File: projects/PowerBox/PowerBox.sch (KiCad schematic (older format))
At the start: 45 parts, among them CON1 USB-MICRO, CON2 USB-MICRO, IC1 OPAMP-DUALU, IC2 ATTINY85-S, P1 CONN_2, P2 CONN_2, P3 CONN_1, P4 CONN_1, P5 CONN_1, P6 CONN_1, P7 CONN_3X2, U1 74HC595, U2 74HC595, U3 INA169

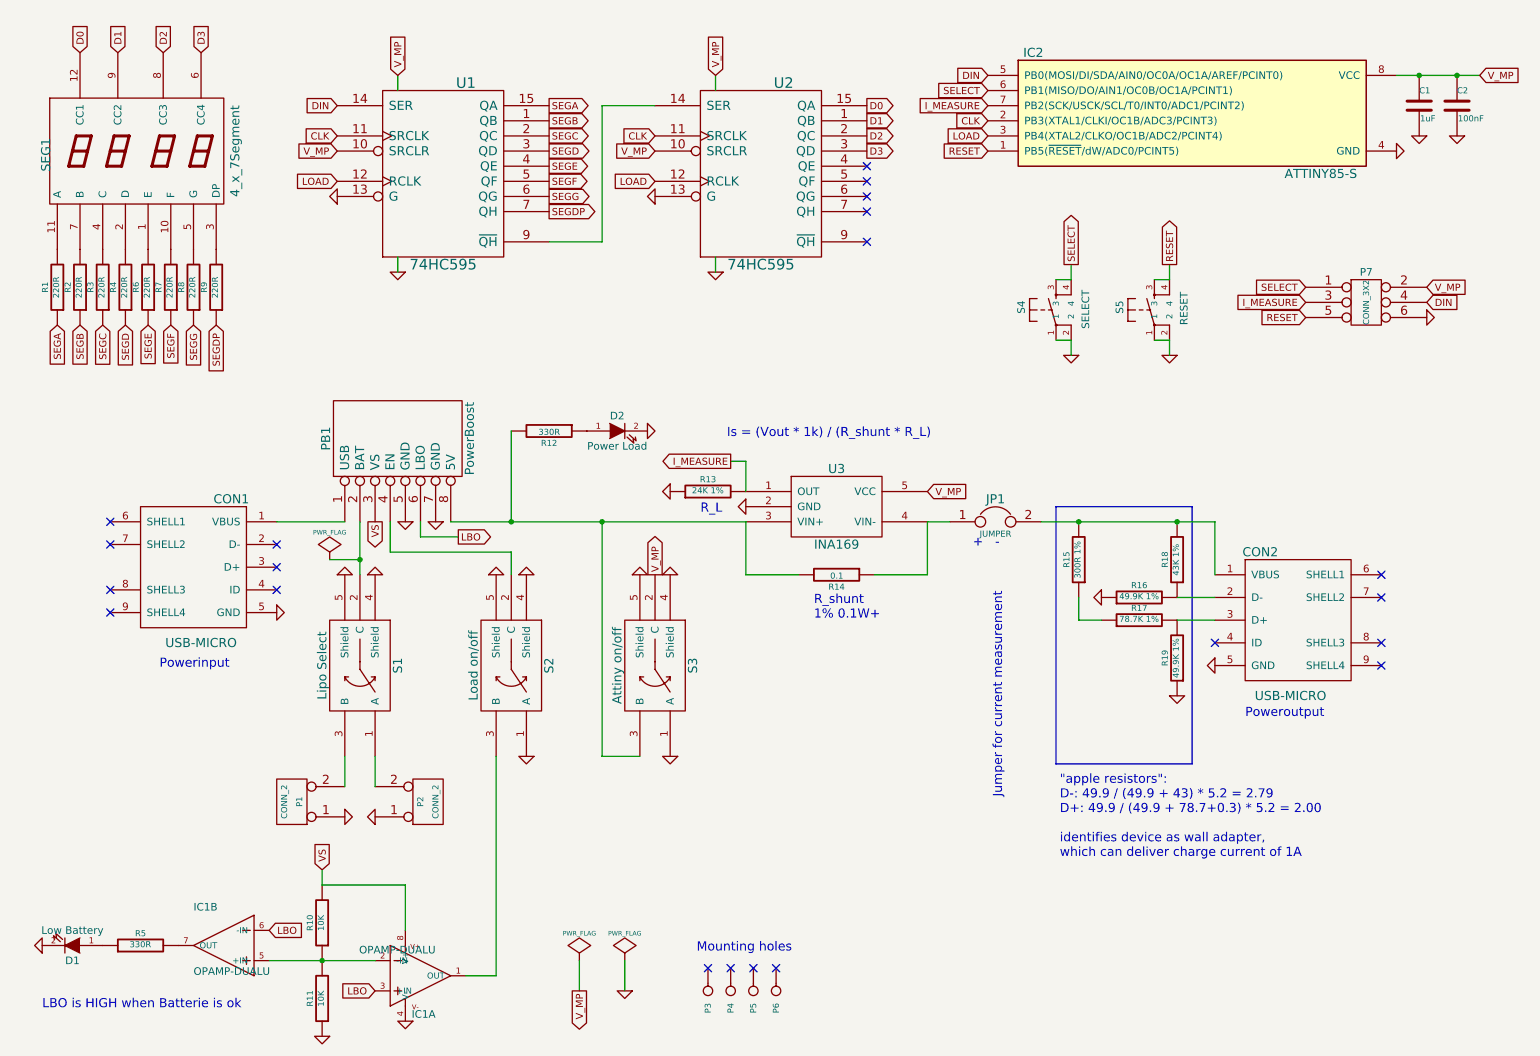
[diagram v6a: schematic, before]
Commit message: attiny replaced with arduino leonardo clone
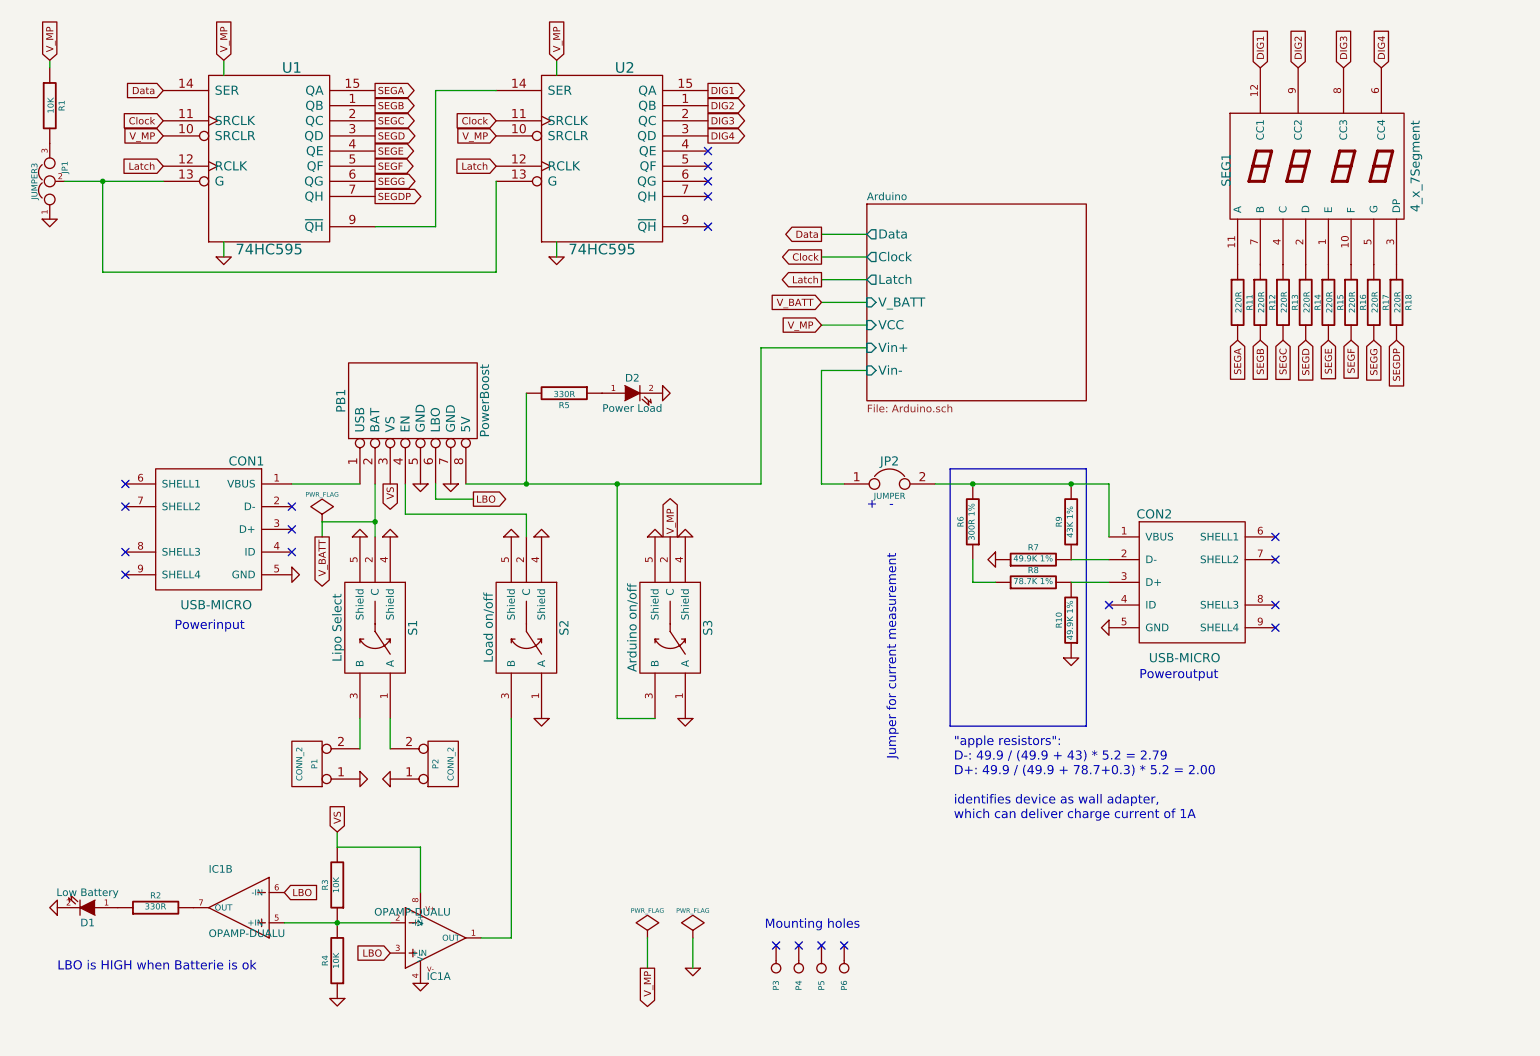
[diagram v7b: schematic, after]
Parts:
- removed C1: 1uF, symbol C
- removed C2: 100nF, symbol C
- removed IC2: ATTINY85-S, SO8-200, symbol ATTINY85-S
- removed P7: CONN_3X2, symbol CONN_3X2
- removed R2, R3, R4, R6, R7, R8, R9: 220R, symbol R
- removed S4: SELECT, TACTILE, symbol TAC_SWITCH
- removed S5: RESET, TACTILE, symbol TAC_SWITCH
- removed U3: INA169, symbol INA169
- added JP1: JUMPER3, symbol JUMPER3
- added R11, R12, R15, R16, R17, R18: 220R, symbol R
- R1: value 220R -> 10K
- R13: value 24K 1% -> 220R
- R14: value 0.1 -> 220R
- S3: value Attiny on/off -> Arduino on/off
- renumbered JP1 to JP2, R19 to R10, R5 to R2, R10 to R3, R11 to R4, R12 to R5, R15 to R6, R16 to R7, R17 to R8, R18 to R9
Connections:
- net I_MEASURE is gone; now on net SEGC: R13.2
- net GND: now also JP1.1; no longer R13.1, U1.13 (G), U2.13 (G)
- net SEGA: now also R11.2; no longer R1.1
- net SEGB: now also R12.2
- net SEGD: now also R14.2
- net SEGDP: now also R18.2
- net SEGE: now also R15.2
- net SEGF: now also R16.2
- net SEGG: now also R17.2
- net VCC: now also R1.1
- net at SEG1.1 (E): now also R15.1
- net at SEG1.10 (F): now also R16.1
- net at SEG1.11 (A): now also R11.1; no longer R1.2
- net at SEG1.2 (D): now also R14.1
- net at SEG1.3 (DP): now also R18.1
- net at SEG1.4 (C): now also R13.1
- net at SEG1.5 (G): now also R17.1
- net at SEG1.7 (B): now also R12.1
- net Arduino/Vin-: now reaches JP2.1
- net Arduino/Vin-: no longer R14.1
- net Arduino/Vin+: now reaches PB1.8 (5V), R5.2, S3.3 (B)
- net Arduino/Vin+: no longer R14.2
- net V_BATT: now reaches PB1.2 (BAT), S1.2 (C)
- net CLK renamed Clock
- net D0 renamed DIG1
- net D1 renamed DIG2
- net D2 renamed DIG3
- net D3 renamed DIG4
- net DIN renamed Data
- net LOAD renamed Latch
- new net: JP1.2, U1.13 (G), U2.13 (G)
- new net: JP1.3, R1.2
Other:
- note removed: "Is = (Vout * 1k) / (R_shunt * R_L)"
- note removed: "R_L"
- note removed: "R_shunt\n1% 0.1W+"
- moved on the sheet: CON1, CON2, D1, D2, IC1A, IC1B, JP2, P1, P2, P3, P4, P5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

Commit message: small modifications
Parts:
- renumbered CON1 to CON?, CON2 to CON?, D1 to D?, D2 to D?, IC1 to IC?, JP2 to JP?, JP1 to JP?, P1 to P?, P2 to P?, P6 to P?, P5 to P?, P4 to P?, P3 to P?, PB1 to PB?, R9 to R?, R8 to R?, R10 to R?, R7 to R?, R3 to R?, R4 to R?, R2 to R?, R5 to R?, R6 to R?, R1 to R?, R11 to R?, R12 to R?, R13 to R?, R14 to R?, R15 to R?, R16 to R?, R17 to R?, R18 to R?, S1 to S?, S2 to S?, S3 to S?, SEG1 to SEG?, U1 to U?, U2 to U?
